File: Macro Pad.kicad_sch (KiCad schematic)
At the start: 19 parts, among them U1 Arduino_Pro_Micro

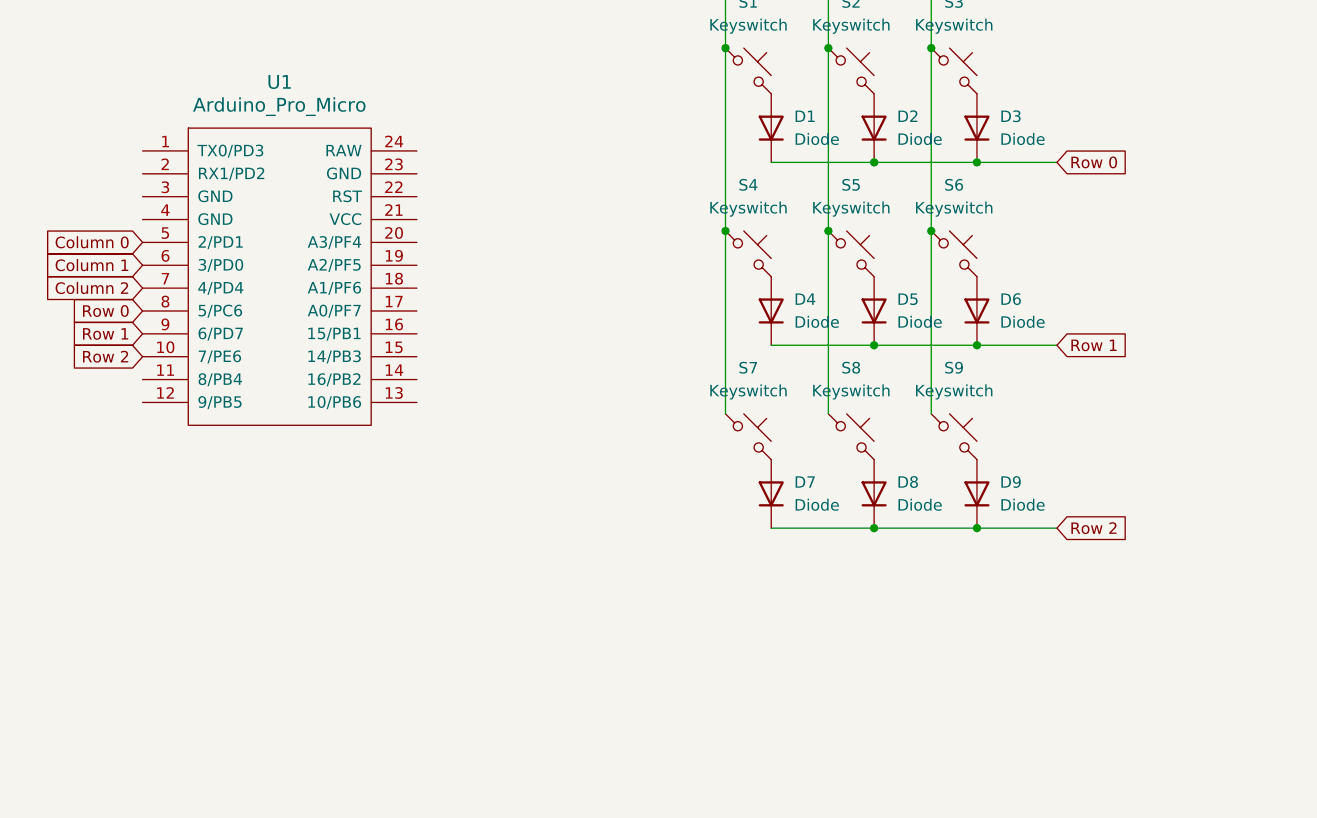
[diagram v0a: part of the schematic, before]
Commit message: Added two rotary encoders
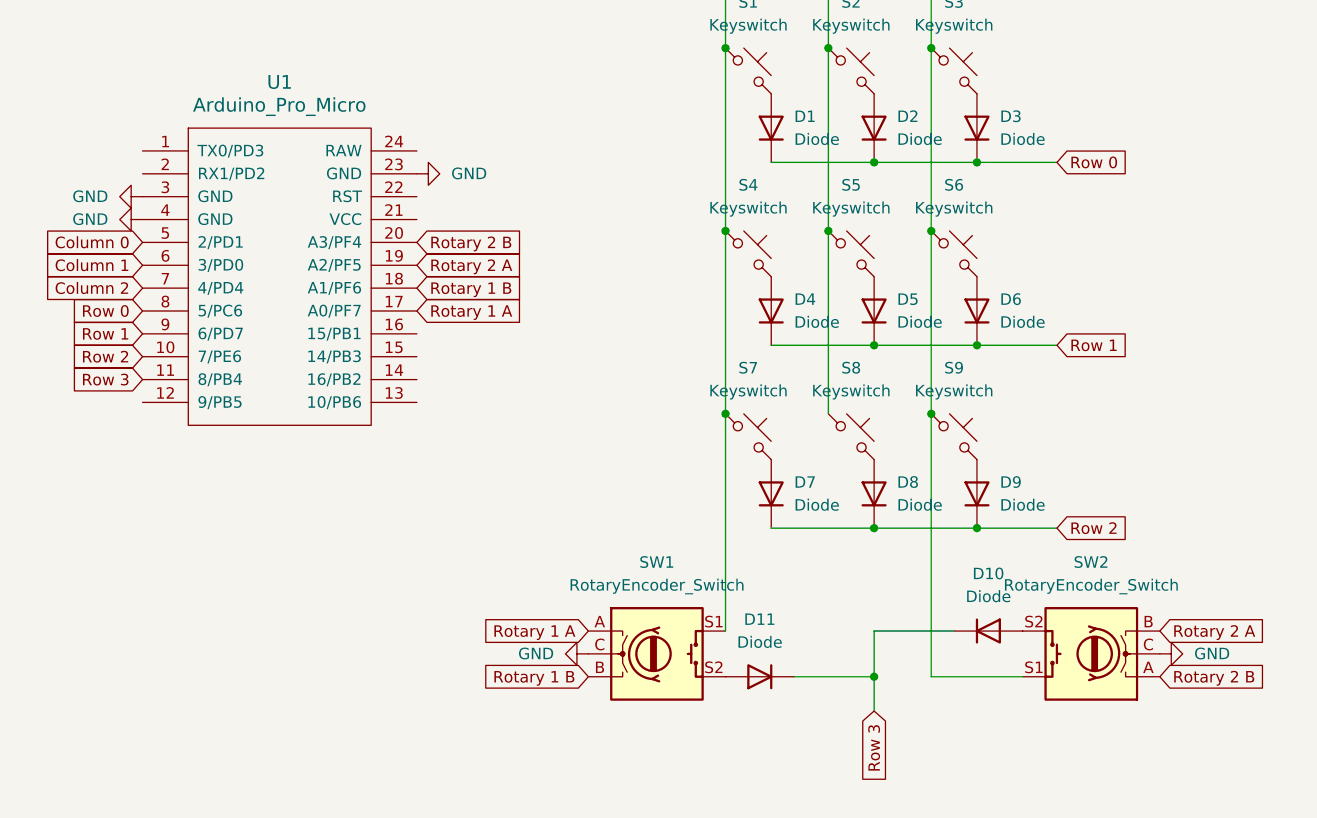
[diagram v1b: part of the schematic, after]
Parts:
- added D10, D11: Diode, ScottoKeebs_Components:Diode_DO-35, symbol ScottoKeebs:Placeholder_Diode
- added SW1, SW2: RotaryEncoder_Switch, Rotary_Encoder:RotaryEncoder_Alps_EC11E-Switch_Vertical_H20mm, symbol Device:RotaryEncoder_Switch
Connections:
- net Column 0: now also SW1.S1
- net Column 2: now also SW2.S1
- net Row 3: now reaches U1.11 (8/PB4)
- net Row 3: now also D10.1 (K), D11.1 (K)
- net Rotary 1 A: now reaches U1.17 (A0/PF7)
- net Rotary 1 A: now also SW1.A
- net Rotary 1 B: now reaches U1.18 (A1/PF6)
- net Rotary 1 B: now also SW1.B
- net Rotary 2 A: now reaches U1.19 (A2/PF5)
- net Rotary 2 A: now also SW2.B
- net Rotary 2 B: now reaches U1.20 (A3/PF4)
- net Rotary 2 B: now also SW2.A
- net GND: now reaches U1.23 (GND)
- net GND: now also U1.3 (GND), U1.4 (GND), SW1.C, SW2.C
- new net: D11.2 (A), SW1.S2
- new net: D10.2 (A), SW2.S2

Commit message: Adding Files
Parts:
- removed D1, D10, D11, D2, D3, D4, D5, D6, D7, D8, D9: Diode, ScottoKeebs_Components:Diode_DO-35, symbol ScottoKeebs:Placeholder_Diode
- removed U1: Arduino_Pro_Micro, ScottoKeebs_MCU:Arduino_Pro_Micro, symbol ScottoKeebs:MCU_Arduino_Pro_Micro
- added C1, C2: 100nF, Capacitor_SMD:C_0603_1608Metric, symbol Device:C
- added C3: 4.7uF, Capacitor_SMD:C_0603_1608Metric, symbol Device:C
- added C4: 1uF, Capacitor_SMD:C_0603_1608Metric, symbol Device:C
- added J1: USB_C_Receptacle_USB2.0, Connector_USB:USB_C_Receptacle_HRO_TYPE-C-31-M-12, symbol Connector:USB_C_Receptacle_USB2.0
- added J2: OLED, Connector_PinHeader_2.54mm:PinHeader_1x04_P2.54mm_Vertical, symbol Connector:Conn_01x04_Pin
- added J3: Reset, Connector_PinHeader_2.54mm:PinHeader_1x02_P2.54mm_Vertical, symbol Connector:Conn_01x02_Socket
- added R1, R2, R3, R4, R5, R6: 5.1k, Resistor_SMD:R_0603_1608Metric, symbol ScottoKeebs:Placeholder_Resistor
- added R7, R8: 22, Resistor_SMD:R_0603_1608Metric, symbol ScottoKeebs:Placeholder_Resistor
- added S12, S4, S8: Keyswitch, ScottoKeebs_MX:MX_PCB_1.00u, symbol ScottoKeebs:Placeholder_Keyswitch
- added U1: ATMEGA32U4-AUR, Package_QFP:TQFP-44_10x10mm_P0.8mm, symbol MCU_Microchip_ATmega:ATmega32U4-A
- renumbered SW1 to EN1, SW2 to EN2, S8 to S10, S9 to S11, S4 to S5, S5 to S6, S6 to S7, S7 to S9
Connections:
- net GND: now also EN1.S1, EN2.S2, S1.2, S10.2, S11.2, S2.2, S3.2, S5.2, S6.2, S7.2, S9.2, C1.2, C2.2, C3.2, C4.2, J1.A1 (GND), J1.A12 (GND), J1.B1 (GND), J1.B12 (GND), J1.S1 (SHIELD), J2.1 (Pin_1), J3.1 (Pin_1), R1.2, R2.2, R6.2, S12.2, S4.2, S8.2, U1.15 (GND), U1.23 (GND), U1.35 (GND), U1.43 (GND), U1.5 (UGND)
- net Rotary 1 A: now also U1.40 (PF1)
- net Rotary 1 B: now also U1.41 (PF0)
- net Rotary 2 A: now also U1.11 (PB3)
- net Rotary 2 B: now also U1.10 (PB2)
- net S13: now reaches EN1.S2
- net S13: now also U1.1 (PE6)
- removed net Column 0: EN1.S1, S1.1, S5.1, S9.1
- removed net Column 1: S10.1, S2.1, S6.1
- removed net Column 2: EN2.S1, S11.1, S3.1, S7.1
- new net: J1.A7 (D-), J1.B7 (D-), R7.1
- new net: J1.A5 (CC1), R1.1
- new net: J1.A6 (D+), J1.B6 (D+), R8.1
- new net: J1.B5 (CC2), R2.1
- new net: R5.1, U1.33 (~{HWB}/PE2)
- new net: C4.1, U1.6 (UCAP)
- new net: R3.2, R4.1
- new net: R5.2, R6.1
- new net +5V: C1.1, C2.1, C3.1, J1.A4 (VBUS), J1.A9 (VBUS), J1.B4 (VBUS), J1.B9 (VBUS), J2.2 (Pin_2), R3.1, U1.14 (VCC), U1.2 (UVCC), U1.24 (AVCC), U1.34 (VCC), U1.44 (AVCC), U1.7 (VBUS)
- new net D+: R8.2, U1.4 (D+)
- new net D-: R7.2, U1.3 (D-)
- new net Reset: J3.2 (Pin_2), R4.2, U1.13 (~{RESET})
- new net S1: S1.1, U1.39 (PF4)
- new net S10: S10.1, U1.28 (PB4)
- new net S11: S11.1, U1.27 (PD7)
- new net S12: S12.1, U1.22 (PD5)
- new net S14: EN2.S1, U1.12 (PB7)
- new net S2: S2.1, U1.30 (PB6)
- new net S3: S3.1, U1.25 (PD4)
- new net S4: S4.1, U1.20 (PD2)
- new net S5: S5.1, U1.38 (PF5)
- new net S6: S6.1, U1.29 (PB5)
- new net S7: S7.1, U1.26 (PD6)
- new net S8: S8.1, U1.21 (PD3)
- new net S9: S9.1, U1.37 (PF6)
- new net SCL: J2.3 (Pin_3), U1.18 (PD0)
- new net SDA: J2.4 (Pin_4), U1.19 (PD1)
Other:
- moved on the sheet: EN1, EN2, S1, S10, S11, S2, S3, S5, S6, S7, S9
